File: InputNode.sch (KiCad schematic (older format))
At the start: 4 parts, among them J6 Conn_01x04_Female

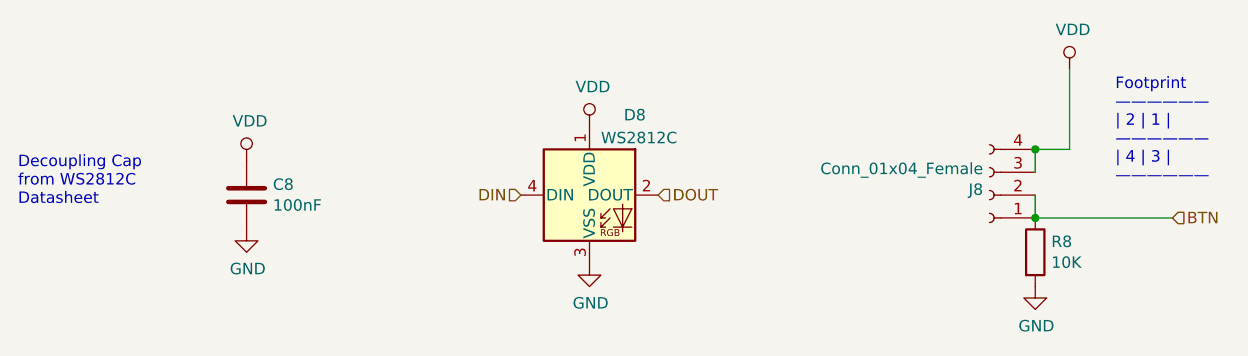
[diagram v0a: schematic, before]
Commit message: updated conns and mounting holes
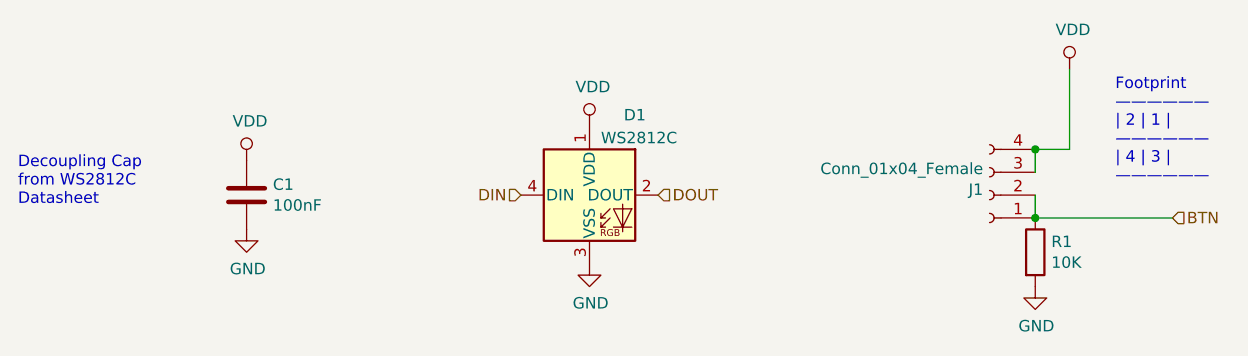
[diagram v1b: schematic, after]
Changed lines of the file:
@@
 AR Path="/61554F98/61493950" Ref="#PWR049"  Part="1"
 AR Path="/61555D68/61493950" Ref="#PWR?"  Part="1"
-F 0 "#PWR049" H 7700 3100 50  0001 C CNN
+F 0 "#PWR05" H 7700 3100 50  0001 C CNN
 F 1 "VDD" H 7715 3423 50  0000 C CNN
 F 2 "" H 7700 3250 50  0001 C CNN
@@
 AR Path="/61554F98/61493958" Ref="D8"  Part="1"
 AR Path="/61555D68/61493958" Ref="D?"  Part="1"
-F 0 "D8" H 5750 4150 50  0000 L CNN
+F 0 "D1" H 5750 4150 50  0000 L CNN
 F 1 "WS2812C" H 5650 4050 50  0000 L CNN
 F 2 "LED_SMD:LED_WS2812B_PLCC4_5.0x5.0mm_P3.2mm" H 5650 3500 50  0001 L TNN
@@
 AR Path="/61554F98/61495684" Ref="#PWR048"  Part="1"
 AR Path="/61555D68/61495684" Ref="#PWR?"  Part="1"
-F 0 "#PWR048" H 5600 3850 50  0001 C CNN
+F 0 "#PWR04" H 5600 3850 50  0001 C CNN
 F 1 "GND" H 5605 3927 50  0000 C CNN
 F 2 "" H 5600 4100 50  0001 C CNN
@@
 AR Path="/61554F98/61495D51" Ref="#PWR047"  Part="1"
 AR Path="/61555D68/61495D51" Ref="#PWR?"  Part="1"
-F 0 "#PWR047" H 5600 3350 50  0001 C CNN
+F 0 "#PWR03" H 5600 3350 50  0001 C CNN
 F 1 "VDD" H 5615 3673 50  0000 C CNN
 F 2 "" H 5600 3500 50  0001 C CNN
@@
 AR Path="/61554F98/614A34FE" Ref="C8"  Part="1"
 AR Path="/61555D68/614A34FE" Ref="C?"  Part="1"
-F 0 "C8" H 4215 3846 50  0000 L CNN
+F 0 "C1" H 4215 3846 50  0000 L CNN
 F 1 "100nF" H 4215 3755 50  0000 L CNN
 F 2 "Capacitor_SMD:C_0805_2012Metric_Pad1.15x1.40mm_HandSolder" H 4138 3650 50  0001 C CNN
@@
 AR Path="/61554F98/614A4287" Ref="#PWR046"  Part="1"
 AR Path="/61555D68/614A4287" Ref="#PWR?"  Part="1"
-F 0 "#PWR046" H 4100 3700 50  0001 C CNN
+F 0 "#PWR08" H 4100 3700 50  0001 C CNN
 F 1 "GND" H 4105 3777 50  0000 C CNN
 F 2 "" H 4100 3950 50  0001 C CNN
@@
 AR Path="/61554F98/614A4795" Ref="#PWR045"  Part="1"
 AR Path="/61555D68/614A4795" Ref="#PWR?"  Part="1"
-F 0 "#PWR045" H 4100 3500 50  0001 C CNN
+F 0 "#PWR07" H 4100 3500 50  0001 C CNN
 F 1 "VDD" H 4115 3823 50  0000 C CNN
 F 2 "" H 4100 3650 50  0001 C CNN
@@
 AR Path="/61554F92/6156DDAC" Ref="J7"  Part="1"
 AR Path="/61554F98/6156DDAC" Ref="J8"  Part="1"
-F 0 "J8" H 7378 3776 50  0000 L CNN
+F 0 "J1" H 7378 3776 50  0000 L CNN
 F 1 "Conn_01x04_Female" H 7378 3685 50  0000 L CNN
 F 2 "Connector_PinSocket_2.54mm:PinSocket_2x02_P2.54mm_Vertical" H 7350 3800 50  0001 C CNN
@@
 AR Path="/61552B2D/6160802E" Ref="R6"  Part="1"
 AR Path="/61554F92/6160802E" Ref="R7"  Part="1"
-F 0 "R8" H 7620 4096 50  0000 L CNN
+F 0 "R1" H 7620 4096 50  0000 L CNN
 F 1 "10K" H 7620 4005 50  0000 L CNN
 F 2 "Resistor_SMD:R_0805_2012Metric_Pad1.20x1.40mm_HandSolder" V 7480 4050 50  0001 C CNN
@@
 AR Path="/61554F98/61608726" Ref="#PWR0110"  Part="1"
 AR Path="/61555D68/61608726" Ref="#PWR?"  Part="1"
-F 0 "#PWR0110" H 7550 3950 50  0001 C CNN
+F 0 "#PWR0103" H 7550 3950 50  0001 C CNN
 F 1 "GND" H 7555 4027 50  0000 C CNN
 F 2 "" H 7550 4200 50  0001 C CNN

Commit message: updated hole footprint
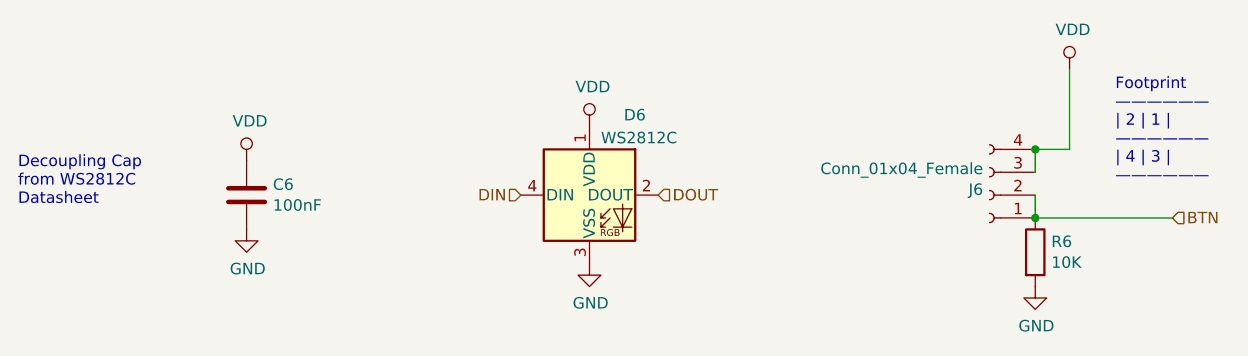
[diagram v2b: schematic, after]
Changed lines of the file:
@@
 $Descr A4 11693 8268
 encoding utf-8
-Sheet 2 9
+Sheet 7 9
 Title ""
 Date ""
@@
 AR Path="/61554F98/61493950" Ref="#PWR049"  Part="1"
 AR Path="/61555D68/61493950" Ref="#PWR?"  Part="1"
-F 0 "#PWR05" H 7700 3100 50  0001 C CNN
+F 0 "#PWR037" H 7700 3100 50  0001 C CNN
 F 1 "VDD" H 7715 3423 50  0000 C CNN
 F 2 "" H 7700 3250 50  0001 C CNN
@@
 AR Path="/61554F98/61493958" Ref="D8"  Part="1"
 AR Path="/61555D68/61493958" Ref="D?"  Part="1"
-F 0 "D1" H 5750 4150 50  0000 L CNN
+F 0 "D6" H 5750 4150 50  0000 L CNN
 F 1 "WS2812C" H 5650 4050 50  0000 L CNN
 F 2 "LED_SMD:LED_WS2812B_PLCC4_5.0x5.0mm_P3.2mm" H 5650 3500 50  0001 L TNN
@@
 AR Path="/61554F98/61495684" Ref="#PWR048"  Part="1"
 AR Path="/61555D68/61495684" Ref="#PWR?"  Part="1"
-F 0 "#PWR04" H 5600 3850 50  0001 C CNN
+F 0 "#PWR036" H 5600 3850 50  0001 C CNN
 F 1 "GND" H 5605 3927 50  0000 C CNN
 F 2 "" H 5600 4100 50  0001 C CNN
@@
 AR Path="/61554F98/61495D51" Ref="#PWR047"  Part="1"
 AR Path="/61555D68/61495D51" Ref="#PWR?"  Part="1"
-F 0 "#PWR03" H 5600 3350 50  0001 C CNN
+F 0 "#PWR035" H 5600 3350 50  0001 C CNN
 F 1 "VDD" H 5615 3673 50  0000 C CNN
 F 2 "" H 5600 3500 50  0001 C CNN
@@
 AR Path="/61554F98/614A34FE" Ref="C8"  Part="1"
 AR Path="/61555D68/614A34FE" Ref="C?"  Part="1"
-F 0 "C1" H 4215 3846 50  0000 L CNN
+F 0 "C6" H 4215 3846 50  0000 L CNN
 F 1 "100nF" H 4215 3755 50  0000 L CNN
 F 2 "Capacitor_SMD:C_0805_2012Metric_Pad1.15x1.40mm_HandSolder" H 4138 3650 50  0001 C CNN
@@
 AR Path="/61554F98/614A4287" Ref="#PWR046"  Part="1"
 AR Path="/61555D68/614A4287" Ref="#PWR?"  Part="1"
-F 0 "#PWR08" H 4100 3700 50  0001 C CNN
+F 0 "#PWR034" H 4100 3700 50  0001 C CNN
 F 1 "GND" H 4105 3777 50  0000 C CNN
 F 2 "" H 4100 3950 50  0001 C CNN
@@
 AR Path="/61554F98/614A4795" Ref="#PWR045"  Part="1"
 AR Path="/61555D68/614A4795" Ref="#PWR?"  Part="1"
-F 0 "#PWR07" H 4100 3500 50  0001 C CNN
+F 0 "#PWR033" H 4100 3500 50  0001 C CNN
 F 1 "VDD" H 4115 3823 50  0000 C CNN
 F 2 "" H 4100 3650 50  0001 C CNN
@@
 AR Path="/61554F92/6156DDAC" Ref="J7"  Part="1"
 AR Path="/61554F98/6156DDAC" Ref="J8"  Part="1"
-F 0 "J1" H 7378 3776 50  0000 L CNN
+F 0 "J6" H 7378 3776 50  0000 L CNN
 F 1 "Conn_01x04_Female" H 7378 3685 50  0000 L CNN
 F 2 "Connector_PinSocket_2.54mm:PinSocket_2x02_P2.54mm_Vertical" H 7350 3800 50  0001 C CNN
@@
 AR Path="/61552B2D/6160802E" Ref="R6"  Part="1"
 AR Path="/61554F92/6160802E" Ref="R7"  Part="1"
-F 0 "R1" H 7620 4096 50  0000 L CNN
+F 0 "R6" H 7620 4096 50  0000 L CNN
 F 1 "10K" H 7620 4005 50  0000 L CNN
 F 2 "Resistor_SMD:R_0805_2012Metric_Pad1.20x1.40mm_HandSolder" V 7480 4050 50  0001 C CNN
@@
 AR Path="/61554F98/61608726" Ref="#PWR0110"  Part="1"
 AR Path="/61555D68/61608726" Ref="#PWR?"  Part="1"
-F 0 "#PWR0103" H 7550 3950 50  0001 C CNN
+F 0 "#PWR0108" H 7550 3950 50  0001 C CNN
 F 1 "GND" H 7555 4027 50  0000 C CNN
 F 2 "" H 7550 4200 50  0001 C CNN
